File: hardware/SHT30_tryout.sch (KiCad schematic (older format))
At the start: 6 parts, among them J1 SHT3x_HEADER, U1 SHT3x-DIS

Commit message: update,
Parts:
- JP1: value SolderJumper_2_Open_round -> SCL_SDA
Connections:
- net NRST: now also RN1.4 (R4.1); no longer RN1.2 (R2.1)
- net SDA: now also RN1.2 (R2.1); no longer RN1.4 (R4.1)
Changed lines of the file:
@@
 U 1 1 5CFA372A
 P 1900 1000
-F 0 "JP1" V 1854 1068 50  0000 L CNN
-F 1 "SolderJumper_2_Open_round" V 1945 1068 50  0000 L CNN
+F 0 "JP1" V 1850 900 50  0000 R CNN
+F 1 "SCL_SDA" V 1900 900 50  0000 R CNN
 F 2 "Jumper:SolderJumper-2_P1.3mm_Open_RoundedPad1.0x1.5mm" H 1900 1000 50  0001 C CNN
 F 3 "~" H 1900 1000 50  0001 C CNN
@@
 Text Label 1850 2050 1    50   ~ 0
 SCL
-Text Label 2150 2050 1    50   ~ 0
+Text Label 1950 2050 1    50   ~ 0
 SDA
 Wire Wire Line
 	1850 1700 1850 2050
 Wire Wire Line
-	2150 1700 2150 2050
+	1950 1700 1950 2050
 $Comp
 L Connector:Conn_01x06_Female J1
@@
 	2100 1200 2150 1200
 Wire Wire Line
-	1950 1850 3100 1850
-Wire Wire Line
-	1950 1700 1950 1850
+	2150 1850 3100 1850
 $Bitmap
 Pos -1000 4000
@@
 Text Label 1800 3050 2    50   ~ 0
 NRST
+Wire Wire Line
+	2150 1700 2150 1850
 $EndSCHEMATC

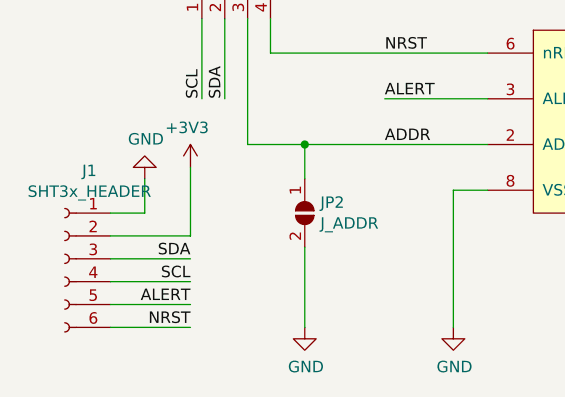
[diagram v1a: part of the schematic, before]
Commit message: update for pin assignment,
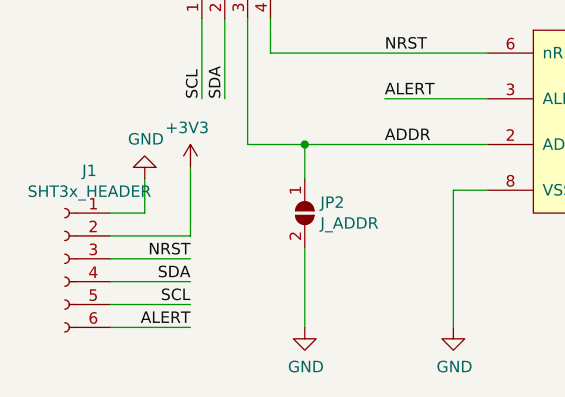
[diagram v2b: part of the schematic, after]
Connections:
- net ALERT: now also J1.6 (Pin_6); no longer J1.5 (Pin_5)
- net NRST: now also J1.3 (Pin_3); no longer J1.6 (Pin_6)
- net SCL: now also J1.5 (Pin_5); no longer J1.4 (Pin_4)
- net SDA: now also J1.4 (Pin_4); no longer J1.3 (Pin_3)
